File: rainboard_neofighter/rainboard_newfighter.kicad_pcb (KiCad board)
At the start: 2 copper layers, 260 x 253.6 mm, 95 parts, among them J1 Conn_01x02, J10 Conn_01x03, J11 SDS-50J, J12 SDS-50J, J13 Conn_01x02, J14 Conn_01x02, J15 Conn_01x02, J16 Conn_01x02, J17 Conn_01x02, J18 Conn_01x02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

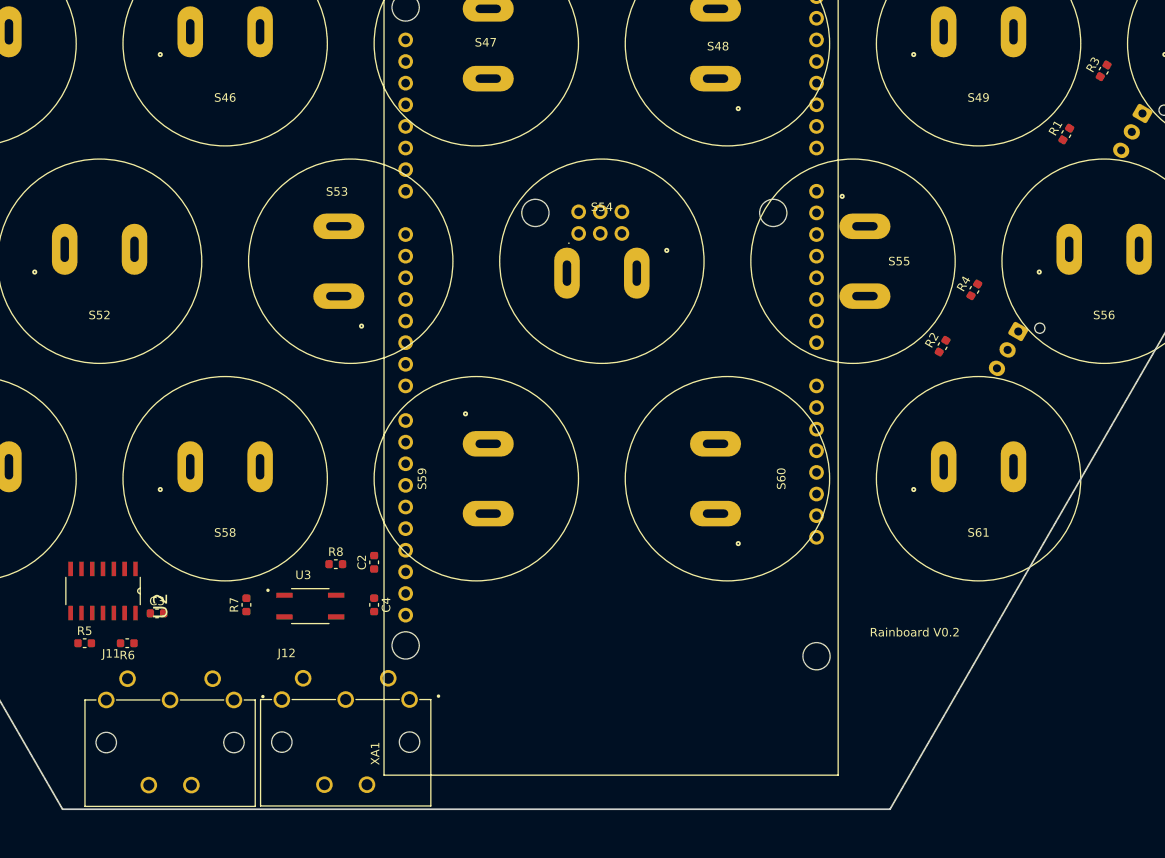
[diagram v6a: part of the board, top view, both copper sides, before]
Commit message: Create analog ground network
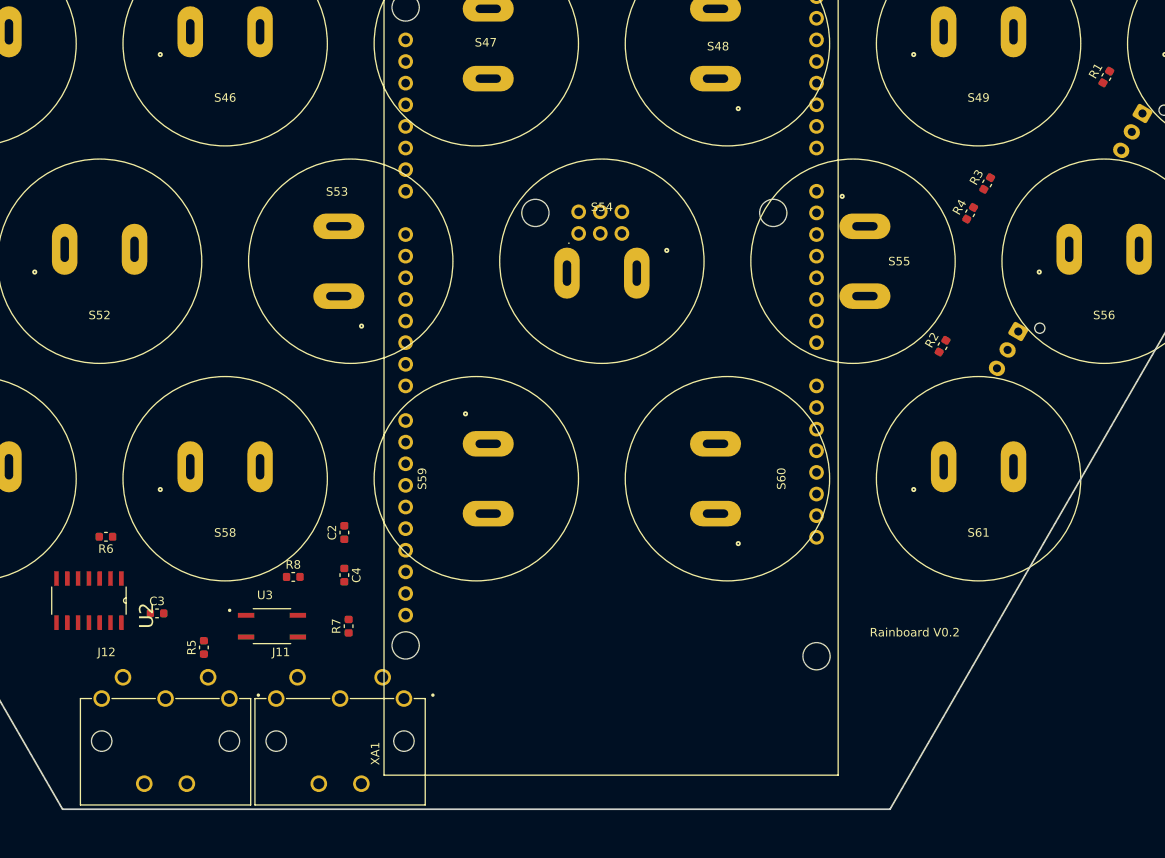
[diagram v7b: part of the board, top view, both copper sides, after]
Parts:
- moved J12 21.2 mm to (-36.5, 128.0)
- moved J11 20.0 mm to (-16.0, 128.0)
- moved R3 19.0 mm to (60.0, 67.5)
- moved R5 14.0 mm to (-32.0, 122.0), turned to 90 degrees
- moved R6 12.7 mm to (-43.5, 109.0)
- moved R7 12.3 mm to (-15.0, 119.5)
- moved R4 9.01 mm to (58.0, 71.0)
- moved R1 8.19 mm to (74.0, 55.0)
- moved R8 5.22 mm to (-21.5, 113.7)
- moved U3 5.08 mm to (-24.0, 119.5)
- moved C2 4.95 mm to (-15.5, 108.5)
- moved C4 4.95 mm to (-15.5, 113.5)
- moved U2 2.01 mm to (-45.5, 116.5)
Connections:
- C2 pad 2: Earth -> GNDA
- R1 pad 2: Earth -> GNDA
- R2 pad 2: Earth -> GNDA
- R4 pad 2: Earth -> GNDA
- XA1 pad 5V3: Net-(XA1-Pad5V3) -> 5V
- XA1 pad 5V4: Net-(XA1-Pad5V4) -> 5V
- XA1 pad GND2: Net-(XA1-PadGND2) -> Earth
- XA1 pad GND3: Net-(XA1-PadGND3) -> Earth
- XA1 pad GND5: Net-(XA1-PadGND5) -> Earth
- XA1 pad GND6: Net-(XA1-PadGND5) -> GNDA

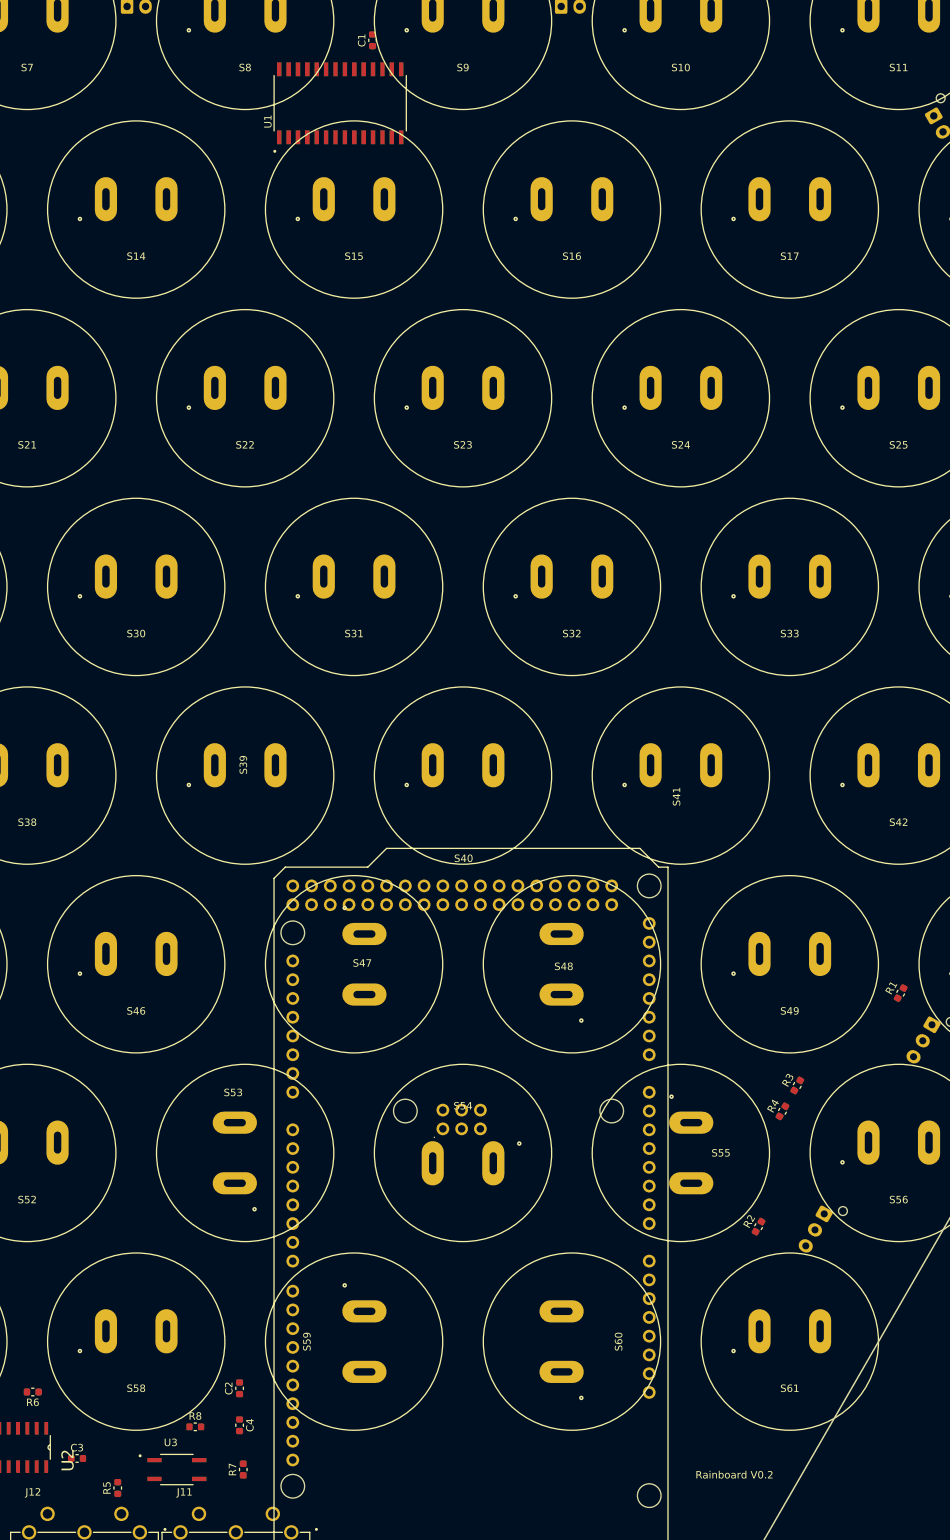
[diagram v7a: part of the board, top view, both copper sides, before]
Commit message: test traces for power and GNDA
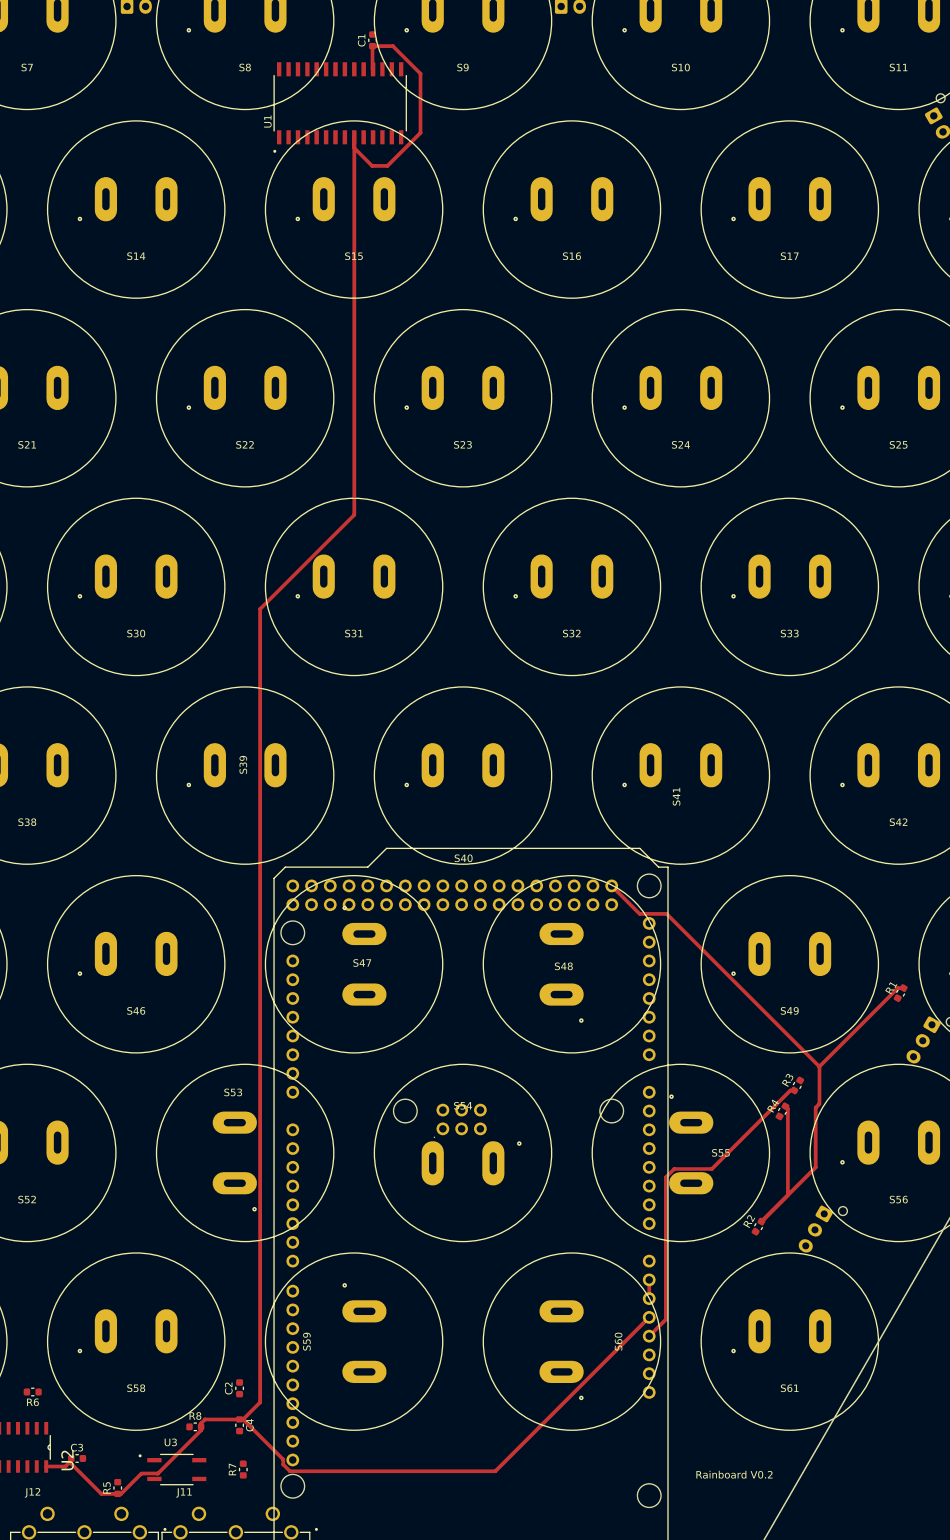
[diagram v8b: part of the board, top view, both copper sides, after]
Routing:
- net 5V: track 0.00 -> 312.6 mm
- net GNDA: track 0.00 -> 95.5 mm
- net 3.3V: track 0.00 -> 44.7 mm
- net Earth: track 0.00 -> 2.54 mm
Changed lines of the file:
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@@
     (thickness 1.6)
     (drawings 8)
-    (tracks 0)
+    (tracks 52)
     (zones 0)
     (modules 95)
@@
   (setup
     (last_trace_width 0.20066)
+    (user_trace_width 0.5)
     (trace_clearance 0.1778)
     (zone_clearance 0.508)
@@
     (effects (font (size 1 1) (thickness 0.15)))
   )
+  (segment (start 39.96 96.36) (end 39.96 93.82) (width 0.5) (layer F.Cu) (net 5))
+  (segment (start -9.591401 118.146099) (end -15.025 112.7125) (width 0.5) (layer F.Cu) (net 69))
+  (segment (start -9.591401 118.823873) (end -9.591401 118.146099) (width 0.5) (layer F.Cu) (net 69))
+  (segment (start -8.683075 119.732199) (end -9.591401 118.823873) (width 0.5) (layer F.Cu) (net 69))
+  (segment (start 19.127801 119.732199) (end -8.683075 119.732199) (width 0.5) (layer F.Cu) (net 69))
+  (segment (start 39.96 98.9) (end 19.127801 119.732199) (width 0.5) (layer F.Cu) (net 69))
+  (segment (start -20.7125 113.2422) (end -20.7125 113.7172) (width 0.5) (layer F.Cu) (net 69))
+  (segment (start -20.1828 112.7125) (end -20.7125 113.2422) (width 0.5) (layer F.Cu) (net 69))
+  (segment (start -15.5 112.7125) (end -20.1828 112.7125) (width 0.5) (layer F.Cu) (net 69))
+  (segment (start -31.525 122.7875) (end -32 122.7875) (width 0.5) (layer F.Cu) (net 69))
+  (segment (start -26.567499 120.047199) (end -28.784699 120.047199) (width 0.5) (layer F.Cu) (net 69))
+  (segment (start -28.784699 120.047199) (end -31.525 122.7875) (width 0.5) (layer F.Cu) (net 69))
+  (segment (start -20.7125 114.1922) (end -26.567499 120.047199) (width 0.5) (layer F.Cu) (net 69))
+  (segment (start -20.7125 113.7172) (end -20.7125 114.1922) (width 0.5) (layer F.Cu) (net 69))
+  (segment (start -32 122.7875) (end -34.2125 122.7875) (width 0.5) (layer F.Cu) (net 69))
+  (segment (start -34.2125 122.7875) (end -38.5 118.5) (width 0.5) (layer F.Cu) (net 69))
+  (segment (start -39.0908 119.0908) (end -41.69 119.0908) (width 0.5) (layer F.Cu) (net 69))
+  (segment (start -38.5 118.5) (end -39.0908 119.0908) (width 0.5) (layer F.Cu) (net 69))
+  (segment (start 2.5 -70.1516) (end 2.5654 -70.0862) (width 0.5) (layer F.Cu) (net 69))
+  (segment (start 2.5 -73.2125) (end 2.5 -70.1516) (width 0.5) (layer F.Cu) (net 69))
+  (segment (start 5.269142 -73.2125) (end 9 -69.481642) (width 0.5) (layer F.Cu) (net 69))
+  (segment (start 2.5 -73.2125) (end 5.269142 -73.2125) (width 0.5) (layer F.Cu) (net 69))
+  (segment (start 9 -61.480758) (end 4.519242 -57) (width 0.5) (layer F.Cu) (net 69))
+  (segment (start 9 -69.481642) (end 9 -61.480758) (width 0.5) (layer F.Cu) (net 69))
+  (segment (start 0.0254 -59.4262) (end 0.0254 -60.8762) (width 0.5) (layer F.Cu) (net 69))
+  (segment (start 2.4516 -57) (end 0.0254 -59.4262) (width 0.5) (layer F.Cu) (net 69))
+  (segment (start 4.519242 -57) (end 2.4516 -57) (width 0.5) (layer F.Cu) (net 69))
+  (segment (start -15.025 112.7125) (end -15.5 112.7125) (width 0.5) (layer F.Cu) (net 69))
+  (segment (start 0.0254 -9.751735) (end -12.720602 2.994267) (width 0.5) (layer F.Cu) (net 69))
+  (segment (start -12.720602 110.408102) (end -15.025 112.7125) (width 0.5) (layer F.Cu) (net 69))
+  (segment (start -12.720602 2.994267) (end -12.720602 110.408102) (width 0.5) (layer F.Cu) (net 69))
+  (segment (start 0.0254 -60.8762) (end 0.0254 -9.751735) (width 0.5) (layer F.Cu) (net 69))
+  (segment (start 48.440523 78.80719) (end 59.065718 68.181995) (width 0.5) (layer F.Cu) (net 88))
+  (segment (start 42.217427 79.936475) (end 43.346712 78.80719) (width 0.5) (layer F.Cu) (net 88))
+  (segment (start 42.217427 99.182573) (end 42.217427 79.936475) (width 0.5) (layer F.Cu) (net 88))
+  (segment (start 43.346712 78.80719) (end 48.440523 78.80719) (width 0.5) (layer F.Cu) (net 88))
+  (segment (start 39.96 101.44) (end 42.217427 99.182573) (width 0.5) (layer F.Cu) (net 88))
+  (segment (start 59.065718 68.181995) (end 59.60625 68.181995) (width 0.5) (layer F.Cu) (net 88))
+  (segment (start 58.741474 82.346681) (end 55.476422 85.611733) (width 0.5) (layer F.Cu) (net 125))
+  (segment (start 58.741474 70.665729) (end 58.741474 82.346681) (width 0.5) (layer F.Cu) (net 125))
+  (segment (start 55.476422 85.611733) (end 55.15615 85.932005) (width 0.5) (layer F.Cu) (net 125))
+  (segment (start 58.39375 70.318005) (end 58.741474 70.665729) (width 0.5) (layer F.Cu) (net 125))
+  (segment (start 73.626414 54.318005) (end 63 64.944419) (width 0.5) (layer F.Cu) (net 125))
+  (segment (start 62.5 70.5) (end 62.5 78.588155) (width 0.5) (layer F.Cu) (net 125))
+  (segment (start 63 64.944419) (end 63 70) (width 0.5) (layer F.Cu) (net 125))
+  (segment (start 62.5 78.588155) (end 55.15615 85.932005) (width 0.5) (layer F.Cu) (net 125))
+  (segment (start 63 70) (end 62.5 70.5) (width 0.5) (layer F.Cu) (net 125))
+  (segment (start 74.39375 54.318005) (end 73.626414 54.318005) (width 0.5) (layer F.Cu) (net 125))
+  (segment (start 35.743599 41.343599) (end 34.88 40.48) (width 0.5) (layer F.Cu) (net 125))
+  (segment (start 38.668599 44.268599) (end 35.743599 41.343599) (width 0.5) (layer F.Cu) (net 125))
+  (segment (start 42.32418 44.268599) (end 38.668599 44.268599) (width 0.5) (layer F.Cu) (net 125))
+  (segment (start 63 64.944419) (end 42.32418 44.268599) (width 0.5) (layer F.Cu) (net 125))
   (zone (net 5) (net_name Earth) (layer B.Cu) (hatch edge 0.508)
     (connect_pads (clearance 0.508))
